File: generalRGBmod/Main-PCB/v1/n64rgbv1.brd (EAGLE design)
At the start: 48.9 x 32.4 mm, 76 parts, among them U1 5M570ZT100C5, U2 THS7374, U3 TLV70018-DDC

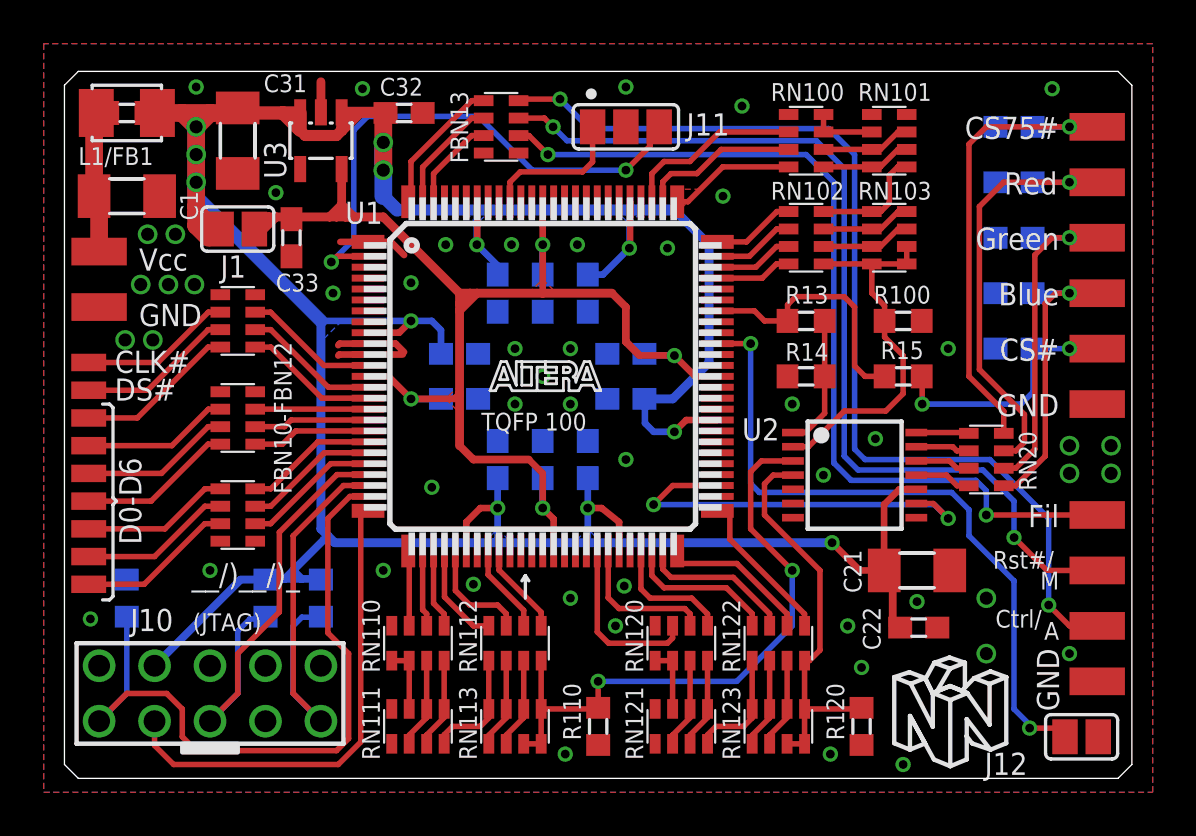
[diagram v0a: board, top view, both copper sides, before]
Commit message: N64RGBv1/v2 misc updates  (thanks to iFixRetro for giving feedback here!!!): - bugfix BOM and silkscreen (N64RGBv2) - silkscreen update to distinguish between MaxII and MaxV setup avoiding assembly mistakes - move power regulator to BOT copper side (N64RGBv1) - additional jumper J1 to select between 240LE and 570LE CPLD (for proper usage of the 5M240ZT)
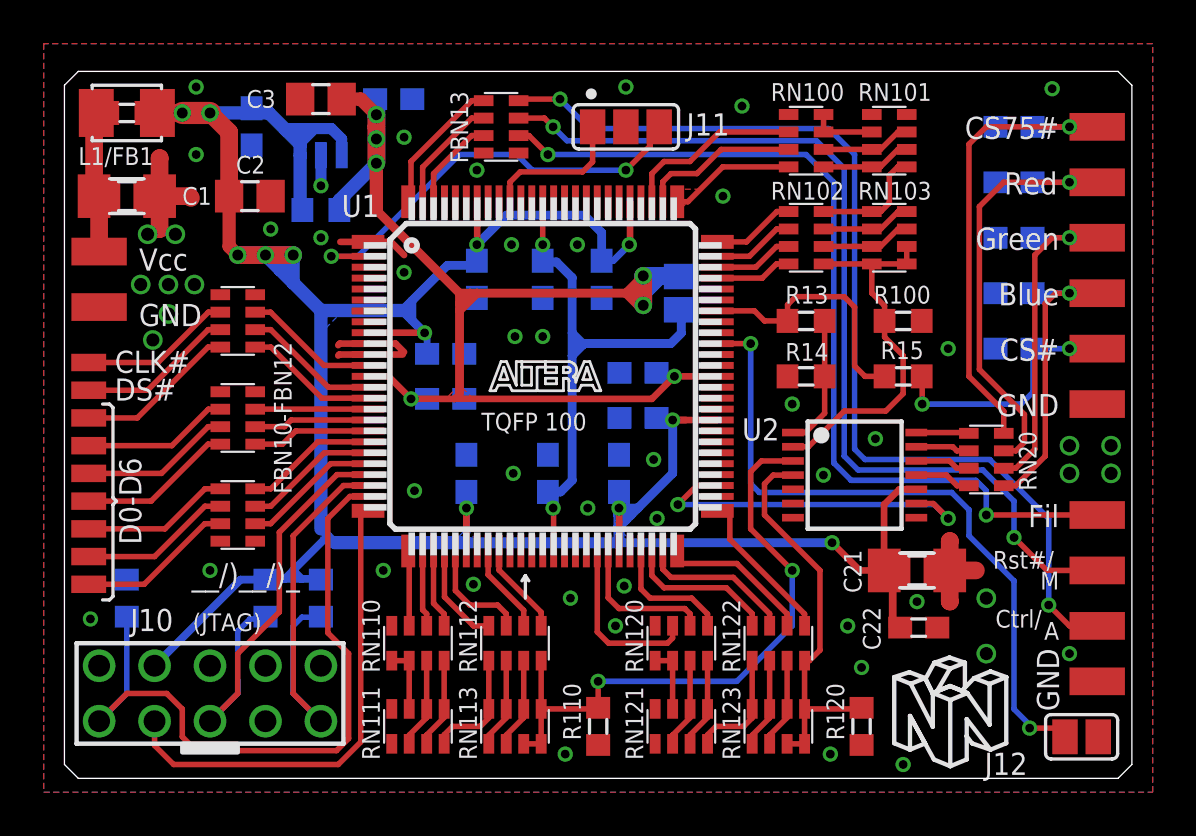
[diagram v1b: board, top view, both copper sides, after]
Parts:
- removed C33: 1u, rcl:C0603
- added C1A, C22A: (no value), rcl:C0805
- added C2, C3: 10u, rcl:C0805
- added FB2: (no value), rcl:R0603
- C31: value 10u -> 1u; device rcl:C1206K -> rcl:C0603
- moved J1 20.5 mm to (29.2, 22.9), flipped to the bottom, turned to 270 degrees
- moved C15 1.56 mm to (19.4, 14.6)
- moved C16 1.56 mm to (26.4, 14.6)
- moved C19 1.14 mm to (19.8, 23.5)
- moved C12 1.03 mm to (27.2, 19.2)
- moved C17 1.03 mm to (27.2, 17.1)
- moved C18 0.90 mm to (25.6, 23.5)
- moved C31 0.90 mm to (9.53, 30.5), flipped to the bottom
- moved C32 0.79 mm to (16.0, 31.8), flipped to the bottom, turned to 180 degrees
- moved C11 0.68 mm to (23.1, 14.6)
- moved C10 0.64 mm to (18.4, 18.0)
- moved C13 0.64 mm to (22.9, 23.5)
- moved C14 0.64 mm to (18.4, 20.1)
- moved U3 0.64 mm to (12.7, 30.5), flipped to the bottom, turned to 0 degrees
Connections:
- new net VCCINT: C11.1, C13.1, J1.2, U1.39, U1.88
- net GND: now also C1A.2, C2.2, C22A.2, C3.2; no longer C33.2
- net N$54: now also C1A.1
- net VCC@1.8V: now also C3.1, C32.1, FB2.2, J1.1; no longer C11.1, C13.1, C33.1, J1.2, U1.39, U1.88
- net VCC@3.3V: now also C2.1, C22A.1, FB2.1; no longer C32.1, J1.1
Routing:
- net VCCINT: track 0.00 -> 25.3 mm, vias 0 -> 2
- net VCC@3.3V: track 164.8 -> 142.9 mm
- net GND: track 10.6 -> 19.5 mm, vias 53 -> 54
- net N$52: track 24.8 -> 20.0 mm
- net VCC@1.8V: track 64.3 -> 61.5 mm, vias 4 -> 7
- net BYP: track 18.8 -> 16.6 mm
- net N$54: track 7.04 -> 7.59 mm
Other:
- board text added: "(570LEs)"
- board text added: "C2"
- board text added: "C3"
- board text added: "Don't use U3,C31,C32 Don't use FB2!!!"
- board text added: "FB2"
- board text added: "MaxII: MaxV:"
- board text added: "N64RGBv1_20180121"
- board text removed: "C33"
- board text removed: "Vers: N64RGBv1 5M_20171211"
